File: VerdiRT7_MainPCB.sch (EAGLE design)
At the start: 183 parts, among them J1 RECEPT_SMD_5-2, J2 RECEPT_SMD_5-2, J4 MOLEX_105027, J5 BM06B-SRSS-TB, J8 BM02B-SRSS-TB, J9 BM02B-ZESS-TBT, Q1 AON7934, Q14 AON7934, Q15 AON7934, Q2 AON7934, Q3 AON7934, Q4 AON7934, Q7 SI7615ADN, SW1 AYZ0102AGRLC, SW3 SKRH, SW4 TACT_SWITCHO, U10 RT9625A, U13 MCP1416, U14 MCP1416, U15 MCP1416, U16 MCP6001, U17 MCP6001, U18 RT9625A, U2 MPU-6500, U3 7408_3, U4 RT9625A, U5 MCP6001, U6 MCP1416, U7 7408_3, U8 7408_3, U9 MCP6001, X1 NX3225

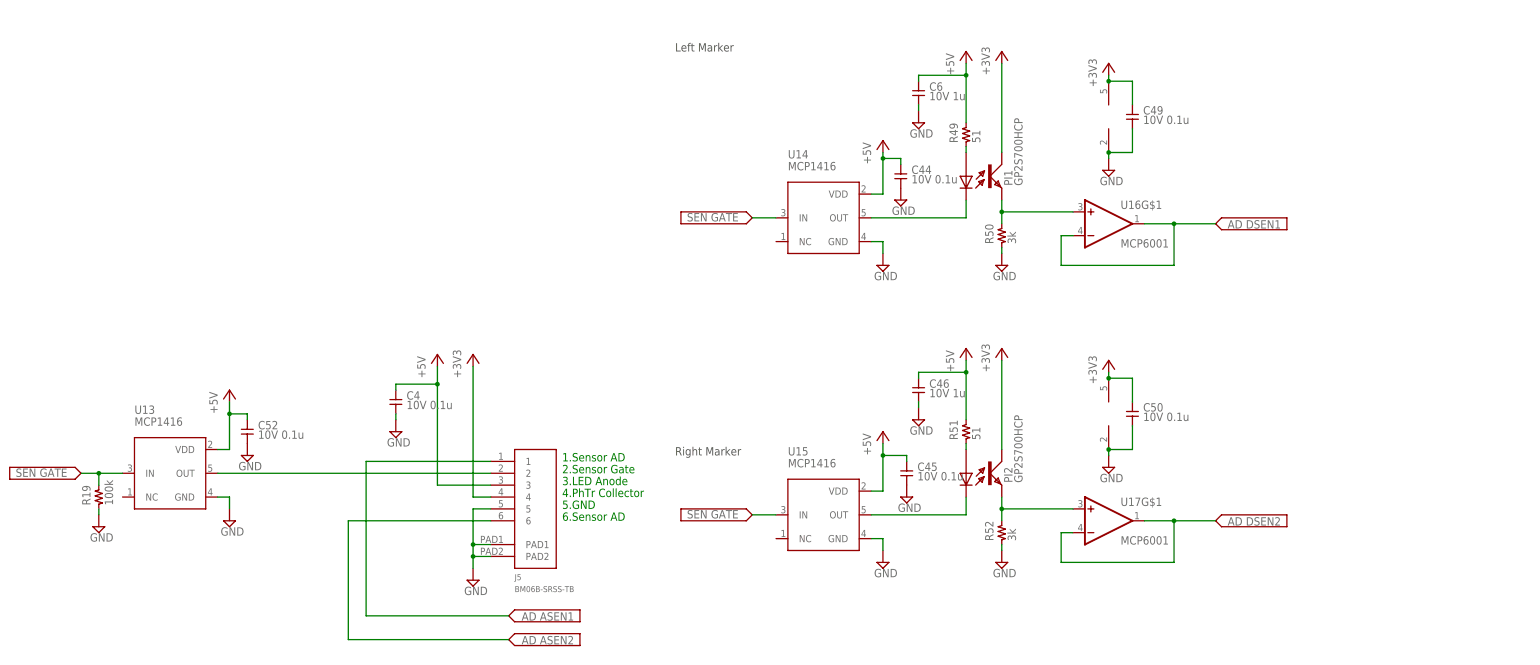
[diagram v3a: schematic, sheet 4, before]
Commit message: updated: コネクタ変更，ディスコンFET 交換
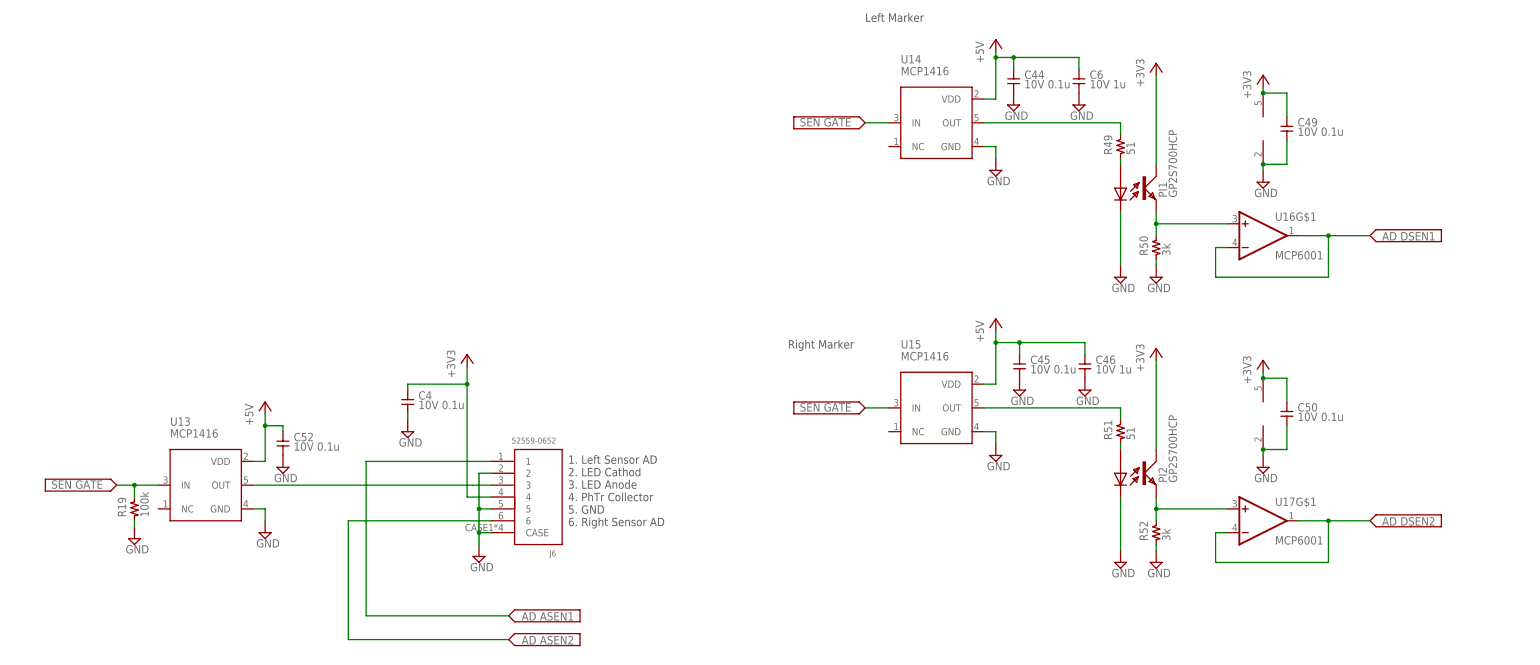
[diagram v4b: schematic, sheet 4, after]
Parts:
- removed J3: (no value), jst_sh:M14B-SRSS-TBTOP
- removed J5: BM06B-SRSS-TB, jst_sh:BM06B-SRSS-TB
- removed J9: BM02B-ZESS-TBT, jst_ze:BM02B-ZESS-TBT
- removed Q14, Q15, Q4: AON7934, MOSFET:AON7934
- removed U2: MPU-6500, gyro:MPU-6500
- added C43: 16V 1u, capacitor:1005
- added C55, C56: 10V 1u, capacitor:1005
- added J13: DF58_2P, Hirose_DF:DF58_2P
- added J15: 503480_0400, molex_503480:503480_0400
- added J16: 503480_0600, molex_503480:503480_0600
- added J6: 52559-0652, molex_52559:52559-0652
- added J7: 503480_1400, molex_503480:503480_1400
- added Q5, Q6, Q8: SIZ322DT, MOSFET:SIZ322DT
- added U19: ICM-20602, ICM-2060x:ICM-20602
- C19, C30: value 16V68u -> 16V33u
- C32, C40: value 16V 68u -> 16V 33u
- Q1, Q2, Q3: value AON7934 -> SIZ322DT; device MOSFET:AON7934 -> MOSFET:SIZ322DT
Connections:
- removed net N$21: J5.2, U13.OUT
- new net IO_SPARE0: J16.3, U1.39_P55/TRDATA3
- new net IO_SPARE1: J16.4, U1.40_P54/TRDATA2
- new net IO_SPARE2: J16.5, U1.41_P53
- new net IO_SPARE3: J15.2, U1.47_PC5
- new net IO_SPARE4: J15.3, U1.48_PC4
- new net N$5: R49.P$2, U14.OUT
- net +3V3: now also C4.P$1, C55.P$1, J16.2, J6.4, J7.8, U19.16_VDD, U19.1_VDDIO; no longer J3.8, J5.4, U2.13_VDD, U2.8_VDDIO
- net +5V: now also C56.P$1, J16.1; no longer C4.P$1, J5.3, R49.P$2, R51.P$2
- net +8V: now also C43.P$1, J15.1, Q1.D1, Q2.D1, Q3.D1, Q5.D1, Q6.D1, Q8.D1; no longer Q1.2_D1, Q1.3_D1, Q1.4_D1, Q1.PAD_S_D1, Q14.2_D1, Q14.3_D1, Q14.4_D1, Q14.PAD_S_D1, Q15.2_D1, Q15.3_D1, Q15.4_D1, Q15.PAD_S_D1, Q2.2_D1, Q2.3_D1, Q2.4_D1, Q2.PAD_S_D1, Q3.2_D1, Q3.3_D1, Q3.4_D1, Q3.PAD_S_D1, Q4.2_D1, Q4.3_D1, Q4.4_D1, Q4.PAD_S_D1
- net AD_ASEN1: now also J6.1; no longer J5.1
- net AD_ASEN2: now also J6.6; no longer J5.6
- net EMLE: now also J7.4; no longer J3.4
- net GND: now also C43.P$2, C55.P$2, C56.P$2, J13.2, J13.CASE, J15.4, J15.CASE, J16.6, J16.CASE, J6.2, J6.5, J6.CASE, J7.12, J7.14, J7.2, J7.CASE, PI1.CATHODE, PI2.CATHODE, Q2.S2, Q3.S2, Q8.S2, U19.10_RESV, U19.11_RESV, U19.12_RESV, U19.13_GND, U19.15_RESV, U19.9_RESV; no longer J3.12, J3.14, J3.2, J3.PAD1, J3.PAD2, J5.5, J5.PAD1, J5.PAD2, J9.1, J9.PAD1, J9.PAD2, Q1.5_S2, Q1.6_S2, Q1.7_S2, Q14.5_S2, Q14.6_S2, Q14.7_S2, Q15.5_S2, Q15.6_S2, Q15.7_S2, Q2.5_S2, Q2.6_S2, Q2.7_S2, Q3.5_S2, Q3.6_S2, Q3.7_S2, Q4.5_S2, Q4.6_S2, Q4.7_S2, U2.18_GND
- net G_FSYNC: now also U19.8_FSYNC; no longer U2.11_FSYNC
- net G_INT: now also U19.6_INT; no longer U2.12_INT
- net MD/FINE: now also J7.7; no longer J3.7
- net MOT1_OUTA: now also Q5.S1D2; no longer Q3.PAD_L_S1D2
- net MOT1_OUTB: now also Q3.S1D2; no longer Q4.PAD_L_S1D2
- net MOT2_OUTA: now also Q6.S1D2; no longer Q1.PAD_L_S1D2
- net MOT2_OUTB: now also Q8.S1D2; no longer Q2.PAD_L_S1D2
- net N$10: now also Q2.G2; no longer Q15.8_G2
- net N$2: now also J6.3, U13.OUT; no longer PI1.CATHODE, U14.OUT
- net N$37: now also Q6.G2; no longer Q1.8_G2
- net N$39: now also Q6.G1; no longer Q1.1_G1
- net N$4: now also U19.14_REGOUT; no longer U2.10_REGOUT
- net N$41: now also Q8.G1; no longer Q2.1_G1
- net N$42: now also Q8.G2; no longer Q2.8_G2
- net N$54: now also R51.P$2; no longer PI2.CATHODE
- net N$61: now also Q5.G2; no longer Q3.8_G2
- net N$65: now also Q1.S1D2; no longer Q14.PAD_L_S1D2
- net N$73: now also Q5.G1; no longer Q3.1_G1
- net N$77: now also Q1.G2; no longer Q14.8_G2
- net N$8: now also Q2.S1D2; no longer Q15.PAD_L_S1D2
- net N$80: now also Q1.G1; no longer Q14.1_G1
- net N$81: now also Q3.G1; no longer Q4.1_G1
- net N$82: now also Q3.G2; no longer Q4.8_G2
- net N$85: now also U19.4_SA0/SDO; no longer U2.9_SDO/AD0
- net N$9: now also Q2.G1; no longer Q15.1_G1
- net RESET: now also J7.13; no longer J3.13
- net SPI_CS0: now also U19.5_NCS; no longer U2.22_NCS
- net SPI_MOSI: now also U19.3_SDA/SDI; no longer U2.24_SDA/SDI
- net SPI_SCK: now also U19.2_SCL/SCLK; no longer U2.23_SCL/SCLK
- net TCK: now also J7.1; no longer J3.1
- net TDI: now also J7.11; no longer J3.11
- net TDO: now also J7.5; no longer J3.5
- net TMS: now also J7.9; no longer J3.9
- net TRST#: now also J7.3; no longer J3.3
- net UB: now also J7.10; no longer J3.10
- net VCC: now also J13.1; no longer J9.2
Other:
- note added: "1. Left Sensor AD 2. LED Cathod 3. LED Anode 4. PhTr Collector 5. GND 6. Right Sensor AD"
- note added: "1. TCK 2. GND 3. TRST# 4. EMLE 5. TDO 6. NC 7. MD/FINED 8. VCC 9. TMS 10. UB 11. TDI 12. GND 13. RES# 14. GND"
- note added: "for I/O Control Spare"
- note added: "for Power Control Spare"
- note removed: "1.Sensor AD"
- note removed: "10: UB"
- note removed: "11: TDI"
- note removed: "12: GND"
- note removed: "13: RES#"
- note removed: "14: GND"
- note removed: "1: TCK"
- note removed: "2.Sensor Gate"
- note removed: "2: GND"
- note removed: "3.LED Anode"
- note removed: "3: TRST#"
- note removed: "4.PhTr Collector"
- note removed: "4: EMLE"
- note removed: "5.GND"
- note removed: "5: TDO"
- note removed: "6.Sensor AD"
- note removed: "6: NC"
- note removed: "7: MD/FINED"
- note removed: "8: VCC"
- note removed: "9: TMS"
- moved on the sheet: C10, C21, C26, C4, C42, C44, C45, C46, C49, C50, C52, C6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

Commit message: updated: DRC 終了
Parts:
- removed CH1: 1X4P, pin_header_2mm:1X4P
- added C57: 10V 0.1u, capacitor:1005
- added J3: DF13-4P-1.25DSA, Hirose_DF:DF13-4P-1.25DSA
- added R64, R74: 100k, resistor:R1005
- added R75: 22, resistor:R1005
- added U2: MR20H40, Memory:MR20H40
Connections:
- new net N$16: R64.P$1, U2.!HOLD
- new net N$21: R74.P$1, U2.!WP
- new net N$45: R75.P$2, U2.DO
- net +3V3: now also C57.P$1, J3.1, R64.P$2, R74.P$2, U2.VDD; no longer CH1.1
- net GND: now also C57.P$2, J13.1, J3.4, Q1.S2, Q5.S2, Q6.S2, U2.PAD, U2.VSS; no longer CH1.4, J13.2
- net RXD2_BTM: now also J3.3; no longer CH1.3
- net SPI_CS1: now also U2.!CS
- net SPI_MISO: now also R75.P$1
- net SPI_MOSI: now also U2.DI
- net SPI_SCK: now also U2.CLK
- net TXD2_BTM: now also J3.2; no longer CH1.2
- net VCC: now also J13.2; no longer J13.1
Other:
- note added: "designed by S.Hirai"
- note removed: "10: I+"
- note removed: "2: Vcc"
- note removed: "3: GND"
- note removed: "4:NC"
- note removed: "9: I-"
- moved on the sheet: B1, C1, C10, C11, C12, C13, C14, C15, C16, C17, C18, C19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

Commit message: updated: リナンバー完了，BOM 完了
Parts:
- removed B1: SMT-0540-S-R, Buzzer:SMT-0540-S-R
- removed C19, C30: 16V33u, capacitor:EEFCX
- removed C32, C40: 16V 33u, capacitor:EEFCX
- removed J1, J2: RECEPT_SMD_5-2, pin_header:RECEPT_SMD_5-2
- removed J11: (no value), jst_sh:BM04B-SRSS-TB
- removed J13: DF58_2P, Hirose_DF:DF58_2P
- removed J4: MOLEX_105027, sd-card:MOLEX_105027
- removed J8: BM02B-SRSS-TB, jst_sh:BM02B-SRSS-TB
- removed LED1, LED2, LED3, LED4, LED5, LED6, LED8: LED1608O, led:LED1608O
- removed Q1, Q2, Q3, Q5, Q6, Q8: SIZ322DT, MOSFET:SIZ322DT
- removed Q7: SI7615ADN, MOSFET:SI7615ADN
- removed R10, R15, R32, R8: 0 (DNP), resistor:R1005
- removed R11, R17: 0, resistor:R1005
- removed R41: 10k, resistor:3216_ARRAY
- removed R43, R53: 4.7k, resistor:R1005
- removed R67, R69, R70(DNP): 22, resistor:R1005
- removed R68: 22, resistor:3216_ARRAY
- removed R73_, R74(DNP): 100k, resistor:R1005
- removed SW3: SKRH, sw1:SKRH
- removed SW4: TACT_SWITCHO, switch:TACT_SWITCHO
- removed U1: (no value), renesas21:RX64M_100
- removed U10, U18, U4: RT9625A, Motor_Driver:RT9625A
- removed U11, U12: (no value), regulator:TLV1117
- removed U13, U14, U15, U6: MCP1416, Motor_Driver:MCP1416
- removed U16, U17, U5, U9: MCP6001, OP-amp:MCP6001
- removed U2: MR20H40, Memory:MR20H40
- removed U3, U7, U8: 7408_3, 74xx-eu:7408_3
- removed VR1: SV01, sensor2:SV01
- removed X1: NX3225, Oscillator:NX3225
- added B101: SMT-0540-T-7-R, Buzzer:SMT-0540-T-7-R
- added C203, C206, C302, C315: EEF-CS1C330R, capacitor:EEF-CS1C330R
- added J102: BM04B-SRSS-TB(LF)(SN), jst_sh:BM04B-SRSS-TB(LF)(SN)
- added J104: 1050270001, sd-card:1050270001
- added J201: DF58-2P-1.2V(21), Hirose_DF:DF58-2P-1.2V(21)
- added J301, J302: 20021321-00010C4LF, pin_header:20021321-00010C4LF
- added J303: BM02B-SRSS-TB(LF)(SN), jst_sh:BM02B-SRSS-TB(LF)(SN)
- added LED101, LED102, LED103, LED104: APHHS1005QBC/D, LED:LED1005
- added LED201, LED203: APHHS1005SYCK, LED:LED1005
- added LED202: APHHS1005ZGC, LED:LED1005
- added Q201: SISA01DN-T1-GE3, MOSFET:SISA01DN-T1-GE3
- added Q301, Q302, Q303, Q304, Q305, Q306: SIZ322DT-T1-GE3, MOSFET:SIZ322DT-T1-GE3
- added R123: 22 (DNP), resistor:R1005
- added R125: 10k, resistor:3216_ARRAY
- added R132: 22, resistor:3216_ARRAY
- added R133, R135: 22, resistor:R1005
- added R139: 100k, resistor:R1005
- added R140: 100k (DNP), resistor:R1005
- added R202, R204: 4.7k, resistor:R1005
- added R307, R309, R314, R319: 0 (DNP), resistor:R1005
- added R311, R317: 0, resistor:R1005
- added SW101: SKRHABE010, sw1:SKRHABE010
- added SW102: SKQYACE010, switch:SKQYACE010
- added U101, U401, U403, U404: MCP1416T-E/OT, Motor_Driver:MCP1416T-E/OT
- added U102, U103, U402, U405: MCP6001T-I/LT, OP-amp:MCP6001T-I/LT
- added U104: R5F564MLDDFP#V1-ND, renesas21:R5F564MLDDFP#V1-ND
- added U105: MR20H40CDF, Memory:MR20H40CDF
- added U201: TLV1117-50CDRJR, regulator:TLV1117-50CDRJR
- added U202: TLV1117-33CDRJR, regulator:TLV1117-33CDRJR
- added U301, U303, U305: 74LVC2G08DC, 74xx-eu:74LVC2G08DC
- added U302, U304, U306: RT9625AZQW, Motor_Driver:RT9625AZQW
- added VR101: SV01A103AEA01, sensor2:SV01A103AEA01
- added X101: NX3225SA-12.000M-STD-CSR-1, Oscillator:NX3225SA-12.000M-STD-CSR-1
- R113, R114: value 20k -> 20k (DNP)
- R117, R118: value 22 -> 22 (DNP)
- renumbered C1 to C204, C10 to C501, C11 to C314, C12 to C201, C13 to C316, C14 to C310, C15 to C104, C16 to C103, C17 to C102, C18 to C106, C2 to C317, C20 to C313, C21 to C502, C22 to C117, C23 to C112, C24 to C113, C25 to C108, C26 to C504, C27 to C111, C28 to C309, C29 to C311, C3 to C115, C31 to C312, C33 to C303, C34 to C307, C35 to C301, C36 to C304, C37 to C205, C38 to C202, C39 to C306, C4 to C406, C41 to C114, C42 to C503, C43 to C119, C44 to C401, C45 to C404, C46 to C405, C47 to C107, C48 to C110, C49 to C403, C5 to C318, C50 to C407, C51 to C101, C52 to C408, C53 to C109, C54 to C105, C55 to C120, C56 to C118, C57 to C116, C6 to C402, C7 to C305, C8 to C308, C9 to C319, D1 to D101, D2 to D102, J15 to J105, J16 to J106, J3 to J103, J6 to J401, J7 to J101, PI1 to PI401, PI2 to PI402, R1 to R110, R12 to R111, R13 to R104, R14 to R107, R16 to R315, R18 to R136, R19 to R404, R2 to R324, R20 to R112, R21 to R109, R22 to R108, R23 to R330, R24 to R327, R25 to R329, R26 to R325, R27 to R318, R28 to R323, R29 to R331, R3 to R502, R30 to R124, R31 to R128, R33 to R316, R34 to R321, R35 to R320, R36 to R322, R37 to R313, R38 to R303, R39 to R312, R4 to R326, R40 to R302, R42 to R203, R44 to R306, R45 to R201, R46 to R304, R47 to R310, R48 to R301, R49 to R401, R5 to R103, R50 to R402, R51 to R403, R52 to R405, R54 to R101, R55 to R105, R56 to R106, R57 to R102, R58 to R120, R59 to R119, R6 to R305, R60 to R116, R61 to R115, R62 to R137, R63 to R501, R64 to R131, R65 to R138, R66 to R129, R7 to R328, R70 to R122, R71 to R121, R71(DNP) to R117, R72 to R126, R72(DNP) to R118, R73 to R127, R74 to R130, R75 to R134, R75(DNP) to R114, R76(DNP) to R113, R9 to R308, SW1 to SW201, U19 to U501
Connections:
- removed net AD_ASEN1: J401.1, U1.89_P45
- removed net AD_ASEN2: J401.6, U1.91_P43
- removed net AD_DSEN1: U1.93_P41, U16G$1.-IN, U16G$1.OUT
- removed net AD_DSEN2: U1.95_P40, U17G$1.-IN, U17G$1.OUT
- removed net MOTOR1: U1.86_PD0, U7G$2.I0
- removed net MOTOR2: U1.85_PD1, U7G$3.I1
- removed net MOTOR3: U1.78_PE0, U3G$2.I0
- removed net MOTOR4: U1.75_PE3, U3G$3.I1
- removed net MOTOR5: U1.74_PE4, U8G$2.I0
- removed net MOTOR6: U1.61_PB0, U8G$3.I1
- removed net MOTOR7: R305.P$1, U1.58_PB2, U10.4_EN2, U10.5_EN1, U4.4_EN2, U4.5_EN1
- removed net MOTOR8: R328.P$1, U1.56_PB4, U18.4_EN2, U18.5_EN1
- removed net PWM_MOTOR1: R137.P$1, U7G$2.I1, U7G$3.I0
- removed net PWM_MOTOR2: R138.P$1, U3G$2.I1, U3G$3.I0
- removed net PWM_MOTOR3: R129.P$1, U8G$2.I1, U8G$3.I0
- removed net TCLK1: R15.P$2, R315.P$2, U1.24_P24
- removed net TCLK2: R17.P$2, R32.P$2, U1.23_P25
- removed net TCLK3: R308.P$2, R8.P$2, U1.26_P22
- removed net TCLK4: R10.P$2, R11.P$2, U1.25_P23
- new net AD_LINE_L_SEN: J401.1, U104.89_P45
- new net AD_LINE_R_SEN: J401.6, U104.91_P43
- new net AD_MARKER_L_SEN: U104.93_P41, U402A.-IN, U402A.OUT
- new net AD_MARKER_R_SEN: U104.95_P40, U405A.-IN, U405A.OUT
- new net DRIVE_MOTOR_EN: R305.P$1, U104.58_PB2, U302.4_EN2, U302.5_EN1, U304.4_EN2, U304.5_EN1
- new net LEFT_MOTOR_CCW: U104.86_PD0, U301A.I0
- new net LEFT_MOTOR_CW: U104.85_PD1, U301B.I1
- new net LEFT_MOTOR_PWM: R137.P$1, U301A.I1, U301B.I0
- new net LEFT_TCLKC: R307.P$2, R308.P$2, U104.26_P22
- new net LEFT_TCLKD: R309.P$2, R311.P$2, U104.25_P23
- new net RIGHT_MOTOR_CCW: U104.78_PE0, U303A.I0
- new net RIGHT_MOTOR_CW: U104.75_PE3, U303B.I1
- new net RIGHT_MOTOR_PWM: R138.P$1, U303A.I1, U303B.I0
- new net RIGHT_TCLKA: R314.P$2, R315.P$2, U104.24_P24
- new net RIGHT_TCLKB: R317.P$2, R319.P$2, U104.23_P25
- new net SENSOR_MOTOR_CCW: U104.74_PE4, U305A.I0
- new net SENSOR_MOTOR_CW: U104.61_PB0, U305B.I1
- new net SENSOR_MOTOR_EN: R328.P$1, U104.56_PB4, U306.4_EN2, U306.5_EN1
- new net SENSOR_MOTOR_PWM: R129.P$1, U305A.I1, U305B.I0
- net +3V3: now also C206.PLUS, J102.1, J104.4_VDD, R139.P$1, R204.P$2, U102G$2.V+, U103G$2.V+, U104.14_VCC, U104.1_AVCC1, U104.35_VCC_USB, U104.60_VCC, U104.96_VREFH0, U104.97_AVCC0, U105.VDD, U202.OUT1, U202.OUT2, U202.OUT3, U202.OUT_PAD, U301PWR.VCC, U303PWR.VCC, U305PWR.VCC, U402G$2.V+, U405G$2.V+, VR101.2; no longer C19.PLUS, J11.1, J4.4_VDD, R53.P$2, R73_.P$1, U1.14_VCC, U1.1_AVCC1, U1.35_VCC_USB, U1.60_VCC, U1.96_VREFH0, U1.97_AVCC0, U12.OUT1, U12.OUT2, U12.OUT3, U12.OUT_PAD, U16G$2.V+, U17G$2.V+, U2.VDD, U3G$1.VCC, U5G$2.V+, U7G$1.VCC, U8G$1.VCC, U9G$2.V+, VR1.2
- net +5V: now also C203.PLUS, J301.P$3, J302.P$3, R125.R1-B, R125.R2-B, R125.R3-B, R125.R4-B, R202.P$2, U101.VDD, U201.OUT1, U201.OUT2, U201.OUT3, U201.OUT_PAD, U401.VDD, U403.VDD, U404.VDD; no longer C30.PLUS, J1.P$3, J2.P$3, R41.R1-B, R41.R2-B, R41.R3-B, R41.R4-B, R43.P$2, U11.OUT1, U11.OUT2, U11.OUT3, U11.OUT_PAD, U13.VDD, U14.VDD, U15.VDD, U6.VDD
- net +8V: now also C302.PLUS, C315.PLUS, Q201.D, Q301.D1, Q302.D1, Q303.D1, Q304.D1, Q305.D1, Q306.D1, U201.IN1, U201.IN2, U201.IN3, U202.IN1, U202.IN2, U202.IN3; no longer C32.PLUS, C40.PLUS, Q1.D1, Q2.D1, Q3.D1, Q5.D1, Q6.D1, Q7.5_D, Q7.9_D, Q8.D1, U11.IN1, U11.IN2, U11.IN3, U12.IN1, U12.IN2, U12.IN3
- net 1_A+: now also J302.P$6; no longer J1.P$6
- net 1_A-: now also J302.P$5, R314.P$1; no longer J1.P$5, R15.P$1
- net 2_B+: now also J302.P$8, R319.P$1; no longer J1.P$8, R32.P$1
- net 2_B-: now also J302.P$7, R317.P$1; no longer J1.P$7, R17.P$1
- net 3_A+: now also J301.P$6; no longer J2.P$6
- net 3_A-: now also J301.P$5, R307.P$1; no longer J2.P$5, R8.P$1
- net 4_B+: now also J301.P$8, R311.P$1; no longer J2.P$8, R11.P$1
- net 4_B-: now also J301.P$7, R309.P$1; no longer J2.P$7, R10.P$1
- net AD_POT: now also U103A.-IN, U103A.OUT, U104.90_P44; no longer U1.90_P44, U5G$1.-IN, U5G$1.OUT
- net AD_POW: now also U102A.-IN, U102A.OUT, U104.92_P42; no longer U1.92_P42, U9G$1.-IN, U9G$1.OUT
- net AD_SUB0: now also U104.88_P46; no longer U1.88_P46
- net AD_SUB1: now also U104.87_P47; no longer U1.87_P47
- net CPU_SD_DAT0: now also R133.P$2, U104.80_PD6; no longer R67.P$2, U1.80_PD6
- net CPU_SPI_MOSI: now also U104.64_PA6; no longer U1.64_PA6
- net CPU_SPI_SCK: now also U104.65_PA5; no longer U1.65_PA5
- net EMLE: now also U104.2_EMLE; no longer U1.2_EMLE
- net GND: now also B101.-, C203.MINUS, C206.MINUS, C302.MINUS, C315.MINUS, J102.4, J102.PAD1, J102.PAD2, J104.6_GND, J201.1, J201.CASE, J301.P$4, J302.P$4, J303.PAD1, J303.PAD2, LED201.K, LED202.K, LED203.K, Q301.S2, Q302.S2, Q303.S2, Q304.S2, Q305.S2, Q306.S2, R140.P$2, SW101.1, SW101.2, SW101.COMMON, SW102.2, U101.GND, U102G$2.V-, U103G$2.V-, U104.12_VSS, U104.38_VSS_USB, U104.3_AVSS1, U104.62_VSS, U104.94_VREFL0, U104.99_AVSS0, U105.PAD, U105.VSS, U201.ADJ/GND, U202.ADJ/GND, U301PWR.GND, U302.13_GND, U302.17_GND, U302.2_GND, U303PWR.GND, U304.13_GND, U304.17_GND, U304.2_GND, U305PWR.GND, U306.13_GND, U306.17_GND, U306.2_GND, U401.GND, U402G$2.V-, U403.GND, U404.GND, U405G$2.V-, VR101.1; no longer B1.-, C19.MINUS, C30.MINUS, C32.MINUS, C40.MINUS, J1.P$4, J11.4, J11.PAD1, J11.PAD2, J13.1, J13.CASE, J2.P$4, J4.6_GND, J8.PAD1, J8.PAD2, LED4.K, LED5.K, LED8.K, Q1.S2, Q2.S2, Q3.S2, Q5.S2, Q6.S2, Q8.S2, R74(DNP).P$2, SW3.1, SW3.2, SW3.COMMON, SW4.2, U1.12_VSS, U1.38_VSS_USB, U1.3_AVSS1, U1.62_VSS, U1.94_VREFL0, U1.99_AVSS0, U10.13_GND, U10.17_GND, U10.2_GND, U11.ADJ/GND, U12.ADJ/GND, U13.GND, U14.GND, U15.GND, U16G$2.V-, U17G$2.V-, U18.13_GND, U18.17_GND, U18.2_GND, U2.PAD, U2.VSS, U3G$1.GND, U4.13_GND, U4.17_GND, U4.2_GND, U5G$2.V-, U6.GND, U7G$1.GND, U8G$1.GND, U9G$2.V-, VR1.1
- net G_FSYNC: now also U104.67_PA3; no longer U1.67_PA3
- net G_INT: now also U104.69_PA1; no longer U1.69_PA1
- net IO_SPARE0: now also U104.39_P55/TRDATA3; no longer U1.39_P55/TRDATA3
- net IO_SPARE1: now also U104.40_P54/TRDATA2; no longer U1.40_P54/TRDATA2
- net IO_SPARE2: now also U104.41_P53; no longer U1.41_P53
- net IO_SPARE3: now also U104.47_PC5; no longer U1.47_PC5
- net IO_SPARE4: now also U104.48_PC4; no longer U1.48_PC4
- net LED0: now also LED101.K, U104.52_PC0; no longer LED1.K, U1.52_PC0
- net LED1: now also LED102.K, U104.51_PC1; no longer LED2.K, U1.51_PC1
- net LED2: now also LED103.K, U104.50_PC2; no longer LED3.K, U1.50_PC2
- net LED3: now also LED104.K, U104.49_PC3; no longer LED6.K, U1.49_PC3
- net LED_SUB0: now also U104.34_P12; no longer U1.34_P12
- net LED_SUB1: now also U104.33_P13; no longer U1.33_P13
- net MD/FINE: now also U104.7_MD/FINED; no longer U1.7_MD/FINED
- net MOT1_OUTA: now also J301.P$2, Q301.S1D2, U302.15_PHASE2; no longer J2.P$2, Q5.S1D2, U10.15_PHASE2
- net MOT1_OUTB: now also J301.P$1, Q302.S1D2, U302.10_PHASE1; no longer J2.P$1, Q3.S1D2, U10.10_PHASE1
- net MOT2_OUTA: now also J302.P$2, Q303.S1D2, U304.15_PHASE2; no longer J1.P$2, Q6.S1D2, U4.15_PHASE2
- net MOT2_OUTB: now also J302.P$1, Q304.S1D2, U304.10_PHASE1; no longer J1.P$1, Q8.S1D2, U4.10_PHASE1
- net N$1: now also Q201.G; no longer Q7.4_G
- net N$10: now also Q306.G2; no longer Q2.G2
- net N$12: now also LED201.A, R202.P$1; no longer LED4.A, R43.P$1
- net N$13: now also U104.11_P37/XTAL, X101.3; no longer U1.11_P37/XTAL, X1.3
- net N$14: now also U304.1_BOOT2; no longer U4.1_BOOT2
- net N$16: now also U105.!HOLD; no longer U2.!HOLD
- net N$17: now also U101.OUT; no longer U6.OUT
- net N$18: now also B101.+; no longer B1.+
- net N$19: now also U402A.+IN; no longer U16G$1.+IN
- net N$2: now also U404.OUT; no longer U13.OUT
- net N$20: now also U103A.+IN, VR101.3, VR101.4; no longer U5G$1.+IN, VR1.3, VR1.4
- net N$21: now also U105.!WP; no longer U2.!WP
- net N$22: now also U304.8_BOOT1; no longer U4.8_BOOT1
- net N$23: now also U104.13_P36/EXTAL, X101.1; no longer U1.13_P36/EXTAL, X1.1
- net N$24: now also J104.5_CLK; no longer J4.5_CLK
- net N$25: now also J104.3_DI/CMD; no longer J4.3_DI/CMD
- net N$26: now also J104.2_-CS/DAT3; no longer J4.2_-CS/DAT3
- net N$27: now also U102A.+IN; no longer U9G$1.+IN
- net N$28: now also J104.1_NC/DAT2; no longer J4.1_NC/DAT2
- net N$3: now also LED202.A; no longer LED5.A
- net N$30: now also U304.12_VCC; no longer U4.12_VCC
- net N$31: now also U303A.O, U304.3_PWM2; no longer U3G$2.O, U4.3_PWM2
- net N$32: now also J104.8_RSV/DAT1; no longer J4.8_RSV/DAT1
- net N$33: now also U303B.O, U304.6_PWM1; no longer U3G$3.O, U4.6_PWM1
- net N$34: now also U304.11_LGATE1; no longer U4.11_LGATE1
- net N$35: now also U304.9_UGATE1; no longer U4.9_UGATE1
- net N$36: now also U304.14_LGATE2; no longer U4.14_LGATE2
- net N$37: now also Q303.G2; no longer Q6.G2
- net N$38: now also U304.16_UGATE2; no longer U4.16_UGATE2
- net N$39: now also Q303.G1; no longer Q6.G1
- net N$41: now also Q304.G1; no longer Q8.G1
- net N$42: now also Q304.G2; no longer Q8.G2
- net N$43: now also U302.1_BOOT2; no longer U10.1_BOOT2
- net N$45: now also U105.DO; no longer U2.DO
- net N$46: now also U302.8_BOOT1; no longer U10.8_BOOT1
- net N$48: now also U302.12_VCC; no longer U10.12_VCC
- net N$49: now also U301A.O, U302.3_PWM2; no longer U10.3_PWM2, U7G$2.O
- net N$5: now also U401.OUT; no longer U14.OUT
- net N$50: now also U301B.O, U302.6_PWM1; no longer U10.6_PWM1, U7G$3.O
- net N$51: now also U302.11_LGATE1; no longer U10.11_LGATE1
- net N$52: now also U302.9_UGATE1; no longer U10.9_UGATE1
- net N$53: now also J104.7_DO/DAT0; no longer J4.7_DO/DAT0
- net N$54: now also U403.OUT; no longer U15.OUT
- net N$55: now also U302.14_LGATE2; no longer U10.14_LGATE2
- net N$56: now also LED101.A, R125.R1-A; no longer LED1.A, R41.R1-A
- net N$57: now also LED102.A, R125.R2-A; no longer LED2.A, R41.R2-A
- net N$58: now also LED103.A, R125.R3-A; no longer LED3.A, R41.R3-A
- net N$59: now also LED104.A, R125.R4-A; no longer LED6.A, R41.R4-A
- net N$6: now also U104.5_VCL; no longer U1.5_VCL
- net N$61: now also Q301.G2; no longer Q5.G2
- net N$62: now also U405A.+IN; no longer U17G$1.+IN
- net N$63: now also U306.1_BOOT2; no longer U18.1_BOOT2
- net N$65: now also J303.1, Q305.S1D2, U306.15_PHASE2; no longer J8.1, Q1.S1D2, U18.15_PHASE2
- net N$66: now also U306.8_BOOT1; no longer U18.8_BOOT1
- net N$68: now also U302.16_UGATE2; no longer U10.16_UGATE2
- net N$69: now also U306.12_VCC; no longer U18.12_VCC
- net N$70: now also U305A.O, U306.3_PWM2; no longer U18.3_PWM2, U8G$2.O
- net N$71: now also U305B.O, U306.6_PWM1; no longer U18.6_PWM1, U8G$3.O
- net N$72: now also U306.11_LGATE1; no longer U18.11_LGATE1
- net N$73: now also Q301.G1; no longer Q5.G1
- net N$74: now also U306.14_LGATE2; no longer U18.14_LGATE2
- net N$75: now also U306.9_UGATE1; no longer U18.9_UGATE1
- net N$77: now also Q305.G2; no longer Q1.G2
- net N$78: now also LED203.A, R204.P$1; no longer LED8.A, R53.P$1
- net N$79: now also U306.16_UGATE2; no longer U18.16_UGATE2
- net N$8: now also J303.2, Q306.S1D2, U306.10_PHASE1; no longer J8.2, Q2.S1D2, U18.10_PHASE1
- net N$80: now also Q305.G1; no longer Q1.G1
- net N$81: now also Q302.G1; no longer Q3.G1
- net N$82: now also Q302.G2; no longer Q3.G2
- net N$83: now also J104.CD1; no longer J4.CD1
- net N$89: now also R132.R4-B, U104.84_PD2; no longer R68.R4-B, U1.84_PD2
- net N$9: now also Q306.G1; no longer Q2.G1
- net N$90: now also R132.R3-B, U104.83_PD3; no longer R68.R3-B, U1.83_PD3
- net N$91: now also R132.R2-B, U104.82_PD4; no longer R68.R2-B, U1.82_PD4
- net N$92: now also R132.R1-B, U104.81_PD5; no longer R68.R1-B, U1.81_PD5
- net N$93: now also R135.P$2, U104.79_PD7; no longer R69.P$2, U1.79_PD7
- net N$94: now also R123.P$2, U104.57_PB3; no longer R70(DNP).P$2, U1.57_PB3
- net N$95: now also U104.37_USB0_DP; no longer U1.37_USB0_DP
- net N$96: now also U104.36_USB0_DM; no longer U1.36_USB0_DM
- net PWM_BUZZER: now also U101.IN, U104.59_PB1; no longer U1.59_PB1, U6.IN
- net PWM_MOT1_MPU: now also U104.77_PE1; no longer U1.77_PE1
- net PWM_MOT2_MPU: now also U104.76_PE2; no longer U1.76_PE2
- net PWM_MOT3_MPU: now also U104.46_PC6; no longer U1.46_PC6
- net PWM_SUB: now also R123.P$1; no longer R70(DNP).P$1
- net RESET: now also SW102.1, U104.10_RES#; no longer SW4.1, U1.10_RES#
- net RXD2_BTM: now also U104.43_P51; no longer U1.43_P51
- net RXD9_OLED: now also J102.3, U104.54_PB6; no longer J11.3, U1.54_PB6
- net SCK2_BTM: now also U104.42_P52; no longer U1.42_P52
- net SCK9_OLED: now also U104.55_PB5; no longer U1.55_PB5
- net SD_CD: now also U104.72_PE6; no longer U1.72_PE6
- net SD_CLK: now also R132.R1-A; no longer R68.R1-A
- net SD_CMD: now also R132.R2-A; no longer R68.R2-A
- net SD_DAT0: now also R133.P$1; no longer R67.P$1
- net SD_DAT1: now also R135.P$1; no longer R69.P$1
- net SD_DAT2: now also R132.R4-A; no longer R68.R4-A
- net SD_DAT3: now also R132.R3-A; no longer R68.R3-A
- net SD_WP: now also U104.71_PE7; no longer U1.71_PE7
- net SEN_GATE: now also U104.32_P14, U401.IN, U403.IN, U404.IN; no longer U1.32_P14, U13.IN, U14.IN, U15.IN
- net SPI_CS0: now also U104.66_PA4; no longer U1.66_PA4
- net SPI_CS1: now also U104.70_PA0, U105.!CS; no longer U1.70_PA0, U2.!CS
- net SPI_CS3: now also U104.68_PA2; no longer U1.68_PA2
- net SPI_MISO: now also U104.63_PA7; no longer U1.63_PA7
- net SPI_MOSI: now also U105.DI; no longer U2.DI
- net SPI_SCK: now also U105.CLK; no longer U2.CLK
- net TACT_A: now also SW101.A, U104.28_P20; no longer SW3.A, U1.28_P20
- net TACT_B: now also SW101.B, U104.29_P17; no longer SW3.B, U1.29_P17
- net TACT_C: now also SW101.C, U104.31_P15; no longer SW3.C, U1.31_P15
- net TACT_CENTER: now also SW101.CENTER, U104.27_P21; no longer SW3.CENTER, U1.27_P21
- net TACT_D: now also SW101.D, U104.30_P16; no longer SW3.D, U1.30_P16
- net TCK: now also U104.21_P27/TCK; no longer U1.21_P27/TCK
- net TDI: now also U104.20_P30/TDI; no longer U1.20_P30/TDI
- net TDO: now also U104.22_P26/TDO; no longer U1.22_P26/TDO
- net TMS: now also U104.19_P31/TMS; no longer U1.19_P31/TMS
- net TRST#: now also U104.16_P34/TRST#; no longer U1.16_P34/TRST#
- net TXD2_BTM: now also U104.44_P50; no longer U1.44_P50
- net TXD9_OLED: now also J102.2, U104.53_PB7; no longer J11.2, U1.53_PB7
- net UB: now also U104.45_PC7/UB; no longer U1.45_PC7/UB
- net UPSEL_NMI: now also R139.P$2, R140.P$1, U104.15_P35/UPSEL/NMI; no longer R73_.P$2, R74(DNP).P$1, U1.15_P35/UPSEL/NMI
- net VCC: now also J201.2, Q201.S; no longer J13.2, Q7.1_S
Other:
- note added: "SENSOR MOTOR"
- note removed: "STEER MOTOR"
